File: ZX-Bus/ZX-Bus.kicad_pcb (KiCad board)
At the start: 2 copper layers, 177 x 146 mm, 51 parts, among them J1 DIP-40 Pins, J2 PLS-3, J3 PLS-6, J4 Power, J5 Main board power, J6 12V, J7 5V, J8 Reset, J9 PLS-2R, U1 Z84C00xxP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

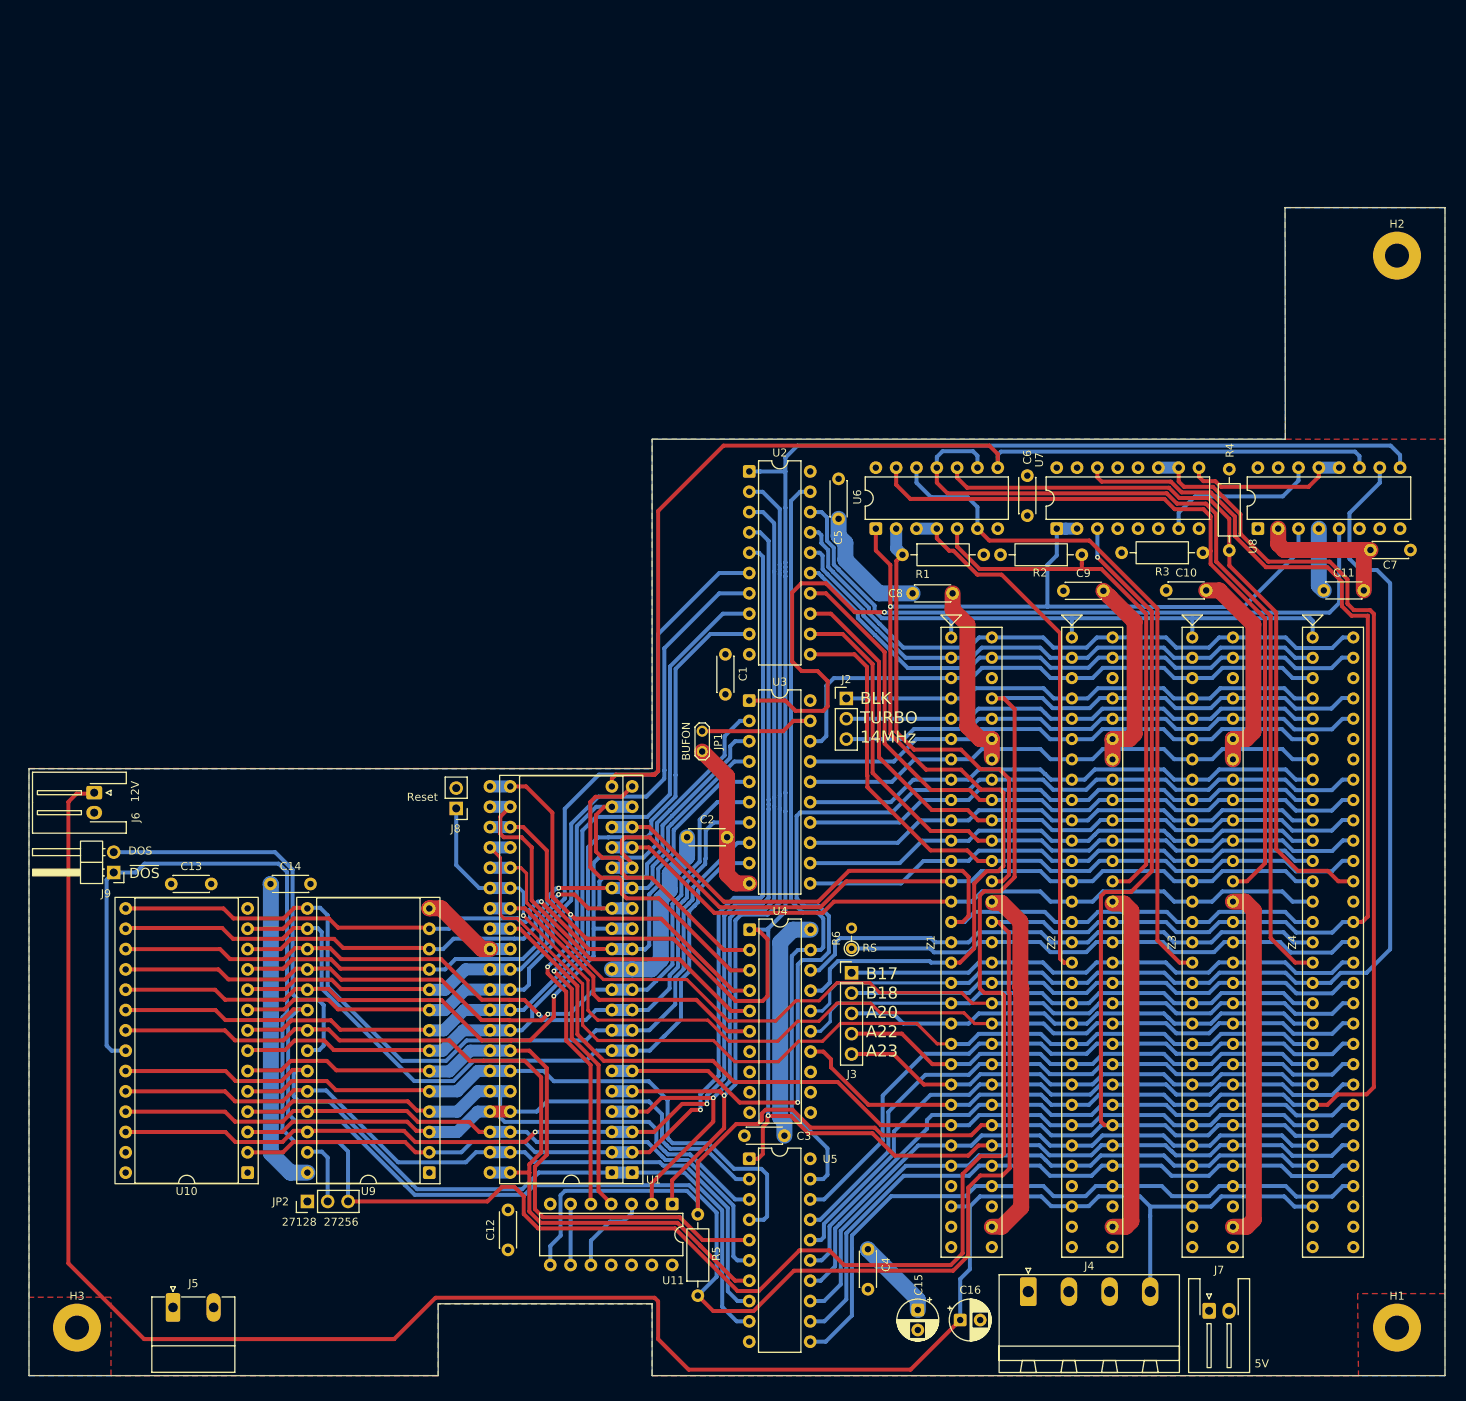
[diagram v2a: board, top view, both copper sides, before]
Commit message: ZX-Bus: Some corrections
Corrected size and layout after verification. SL-62 footprints with proper
courtyards.
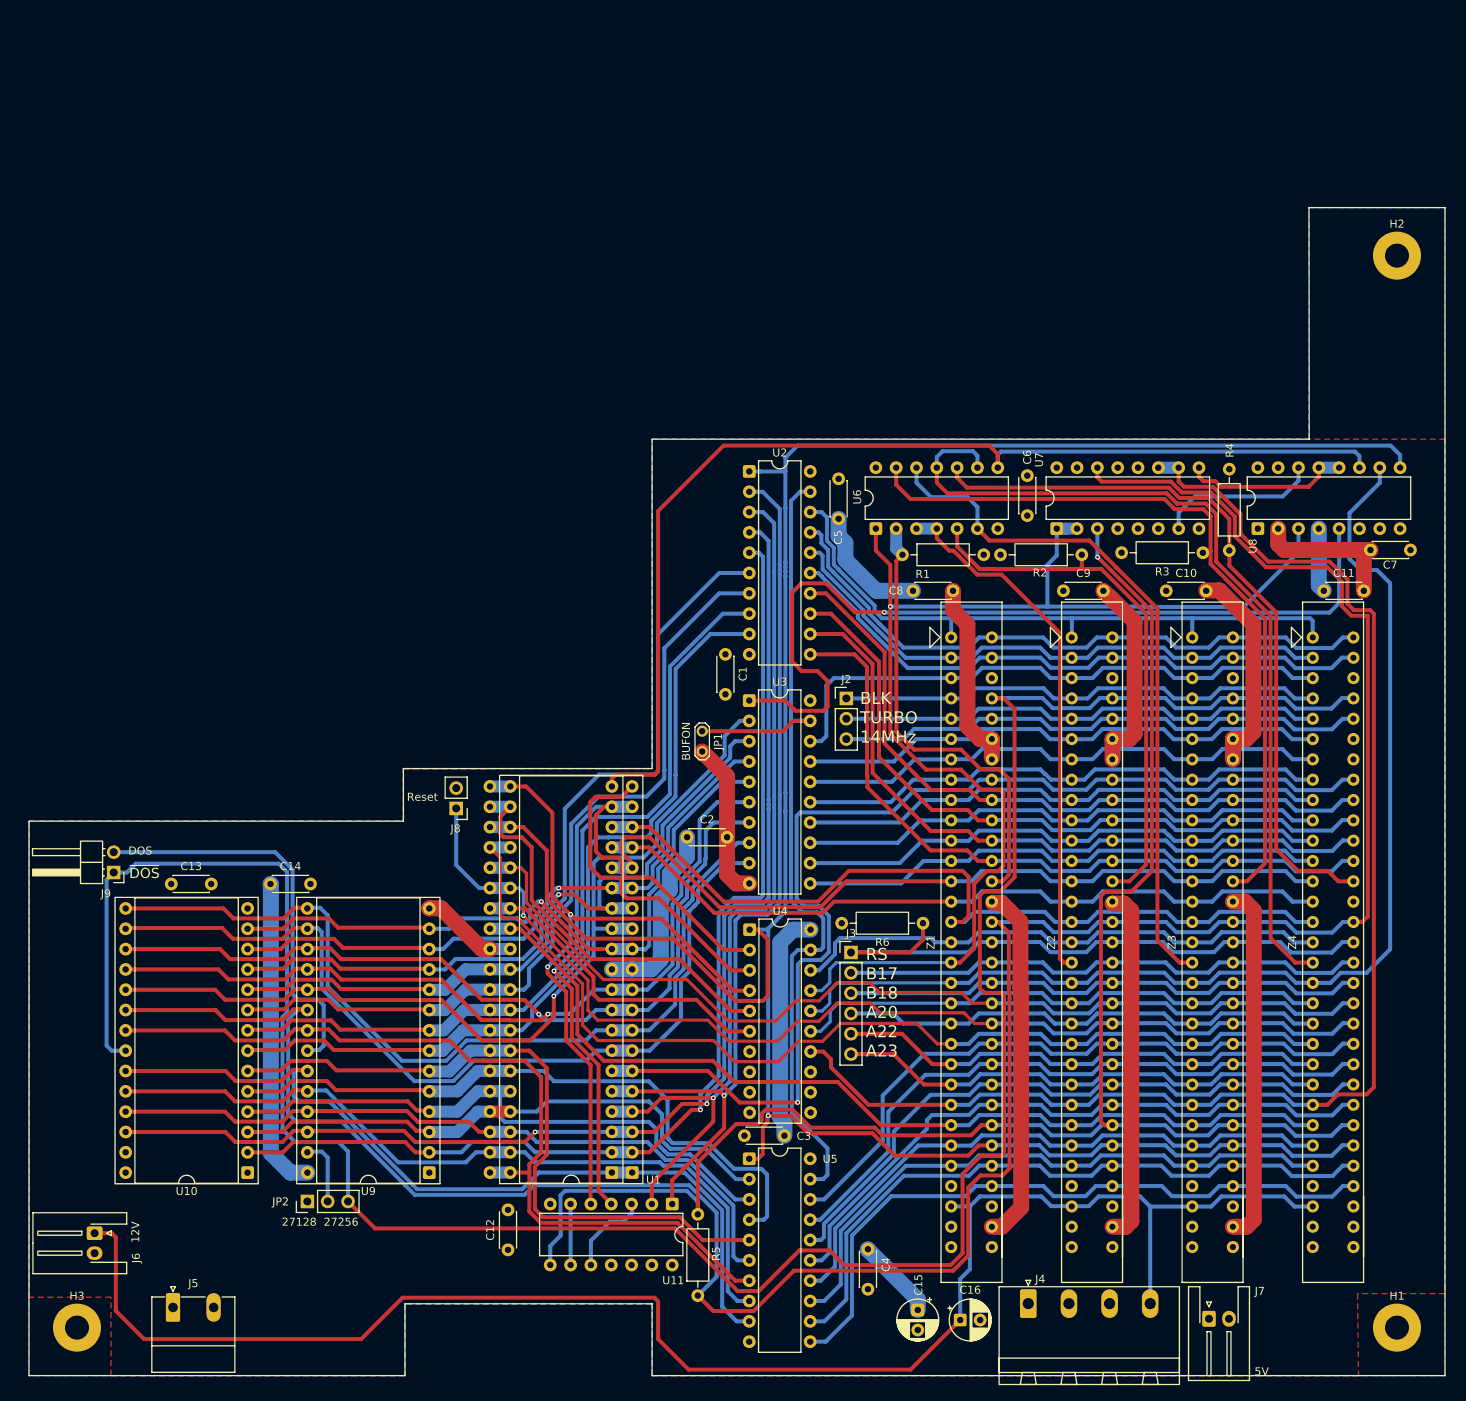
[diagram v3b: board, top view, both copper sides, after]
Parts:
- J3: footprint Connector_PinHeader_2.54mm:PinHeader_1x05_P2.54mm_Vertical -> Connector_PinHeader_2.54mm:PinHeader_1x06_P2.54mm_Vertical
- R6: footprint Resistor_THT:R_Axial_DIN0204_L3.6mm_D1.6mm_P2.54mm_Vertical -> Resistor_THT:R_Axial_DIN0207_L6.3mm_D2.5mm_P10.16mm_Horizontal
- moved J6 55.1 mm to (23.4, 183.0)
- moved R6 9.47 mm to (126.9, 144.3), turned to 180 degrees
- moved J3 2.54 mm to (117.9, 147.9)
- moved J4 1.50 mm to (140.1, 191.8)
- moved J7 1.00 mm to (162.7, 193.7)
- moved C8 0.32 mm to (125.7, 102.7)
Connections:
- J3 pad 1: /B17 -> /RS
- J3 pad 2: /B18 -> /B17
- J3 pad 3: /A20 -> /B18
- J3 pad 4: /A22 -> /A20
- J3 pad 5: /A23 -> /A22
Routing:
- net +12V: track 261.4 -> 205.4 mm
- net /RS: track 66.6 -> 78.2 mm
- net /~{DOS}: track 311.8 -> 309.0 mm
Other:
- outline, holes or cut-outs redrawn
- board text added: "RS B17 B18 A20 A22 A23"
- board text removed: "B17 B18 A20 A22 A23"
- board text removed: "RS"

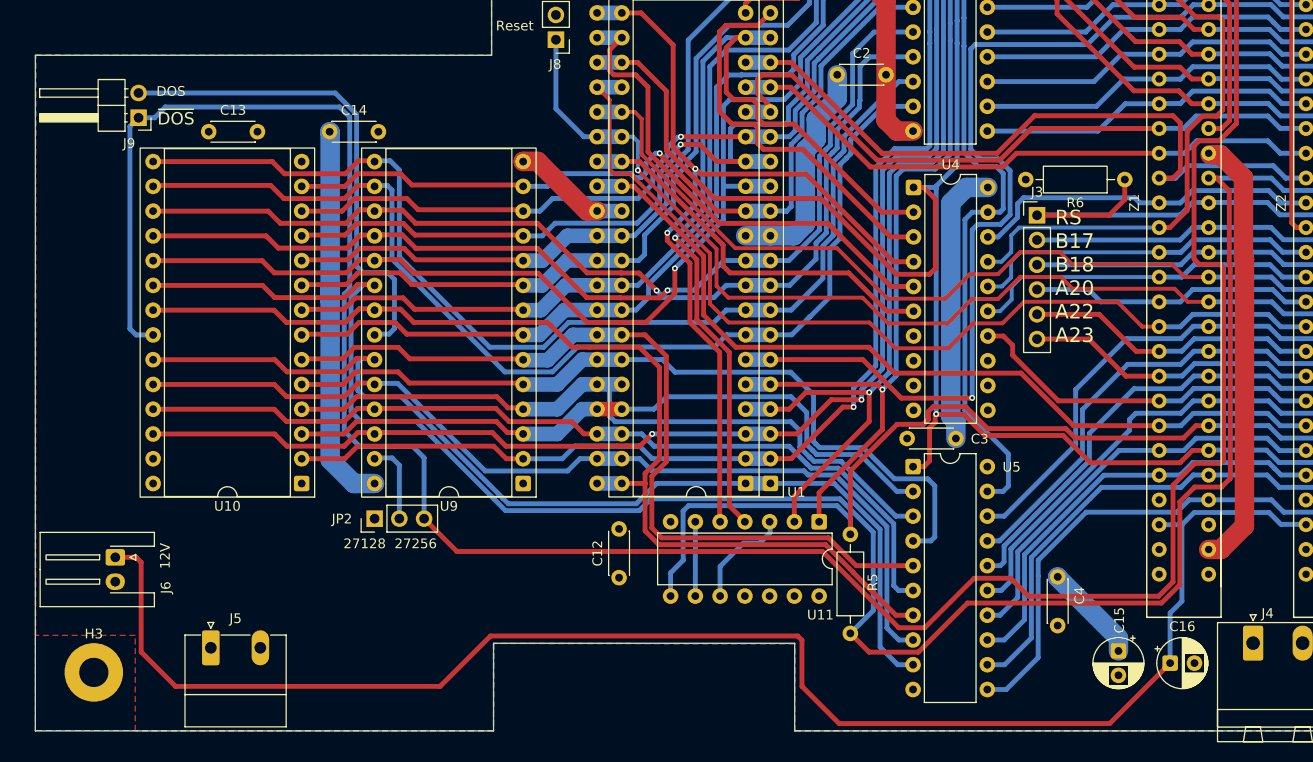
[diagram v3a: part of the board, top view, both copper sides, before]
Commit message: ZX-Bus: More layout improvements
Some ideas
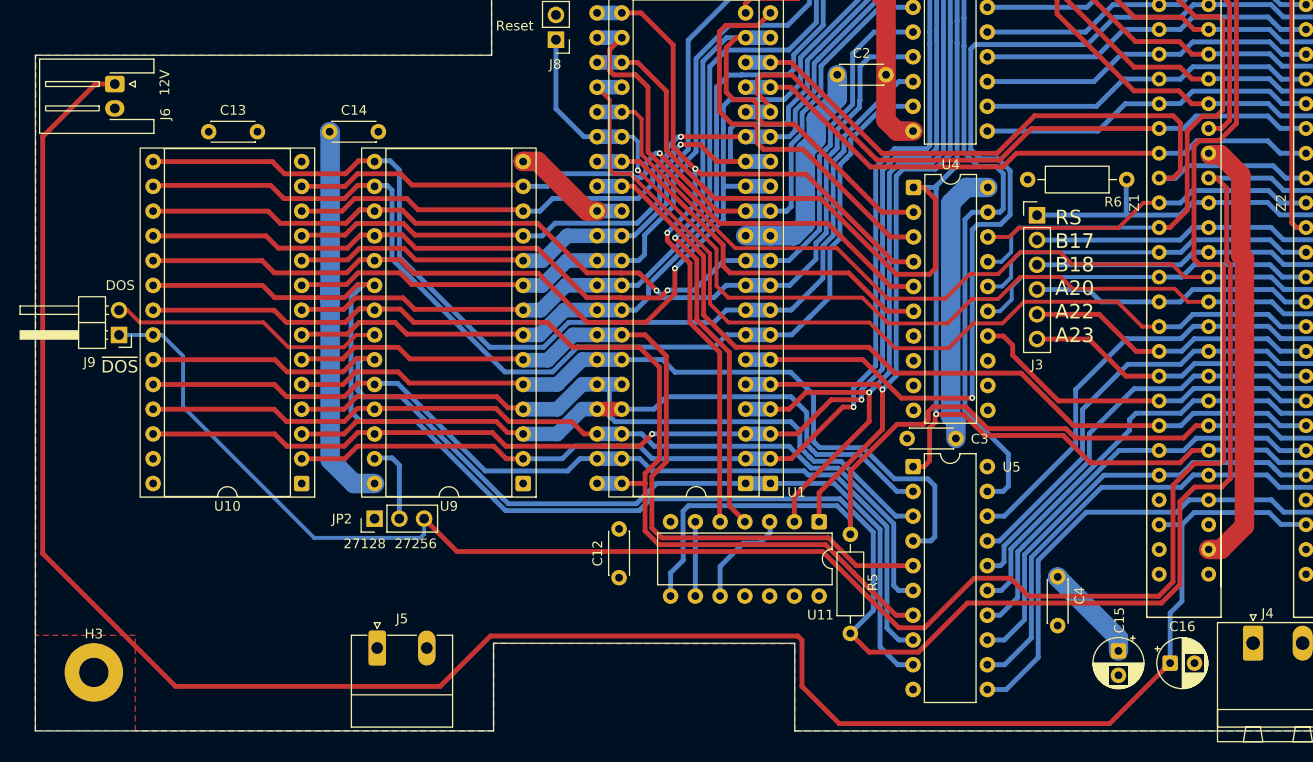
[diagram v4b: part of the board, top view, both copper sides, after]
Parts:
- moved J6 48.6 mm to (23.3, 134.5)
- moved J9 22.4 mm to (23.7, 160.2)
- moved J5 17.1 mm to (50.2, 192.3)
- moved R6 0.20 mm to (127.1, 144.3)
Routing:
- net +12V: track 205.4 -> 260.0 mm
- net /~{DOS}: track 309.0 -> 258.5 mm
- net /DOS: track 50.6 -> 28.3 mm
- net /RS: track 78.2 -> 70.0 mm
- net /~{MREQ}: track 68.6 -> 67.4 mm
